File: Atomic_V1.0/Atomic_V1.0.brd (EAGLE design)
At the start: 20 x 44 mm, 17 parts

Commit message: ..
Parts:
- removed DUMMY1: (no value), Atomic_V1.0:P:EX165Y165D1651
- removed DUMMY11: (no value), Atomic_V1.0:P:EX79Y79D791
- removed DUMMY12, DUMMY13, DUMMY14, DUMMY15, DUMMY16, DUMMY17, DUMMY18, DUMMY20: (no value), Atomic_V1.0:P:RRX47Y47D331
- removed DUMMY19: (no value), Atomic_V1.0:P:SX47Y47D331
- removed DUMMY67: (no value), Atomic_V1.0:P:EX71Y71D511
- removed DUMMY68, DUMMY69: (no value), Atomic_V1.0:P:RRX71Y71D511
- removed DUMMY70: (no value), Atomic_V1.0:P:SX71Y71D511
- removed DUMMY75: (no value), Atomic_V1.0:EF154X154MID1
- removed DUMMY76: (no value), Atomic_V1.0:EF154X154MID2
- added C15: 47 nF, fliegl-wuerth:WCAP-CSGP_0402
- added C17, C19: 100 nF, fliegl-wuerth:WCAP-CSGP_0402
- added D6: 26.2V / 35pF, fliegl-wuerth:WE-TVS_SOT23-3L
- added J1: (no value), Wurth_Connectors_WR-PHD:61300411121
- added J2: (no value), Wurth_Connectors_WR-PHD:61300511121
- added R21, R22: 60.4R 1%, Resistor_smaller_fliegl:WCAP-CSRF_0402
- added U4: TLE9250VSJ, TLE9250VSJ:SOIC127P602X173-8N-V
- added X1: S4P-VH, con-JST VH:S4P-VH
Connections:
- new net +3V3: C19.1, U4.5
- new net +5V: C17.1, U4.3
- new net CAN1_RXD: U4.4
- new net CAN1_TXD: U4.1
- new net CAN_H: D6.2, R22.2, U4.7, X1.3
- new net CAN_L: D6.1, R21.1, U4.6, X1.4
- new net GND: C15.2, C17.2, C19.2, D6.3, U4.2, U4.8, X1.1
- new net N$17: C15.1, R21.2, R22.1
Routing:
- net CAN_L: track 0.00 -> 17.3 mm
- net CAN_H: track 0.00 -> 14.0 mm
- net GND: track 0.00 -> 3.31 mm, vias 0 -> 4
- net N$17: track 0.00 -> 2.54 mm
- net +5V: track 0.00 -> 2.10 mm
- net +3V3: track 0.00 -> 1.78 mm

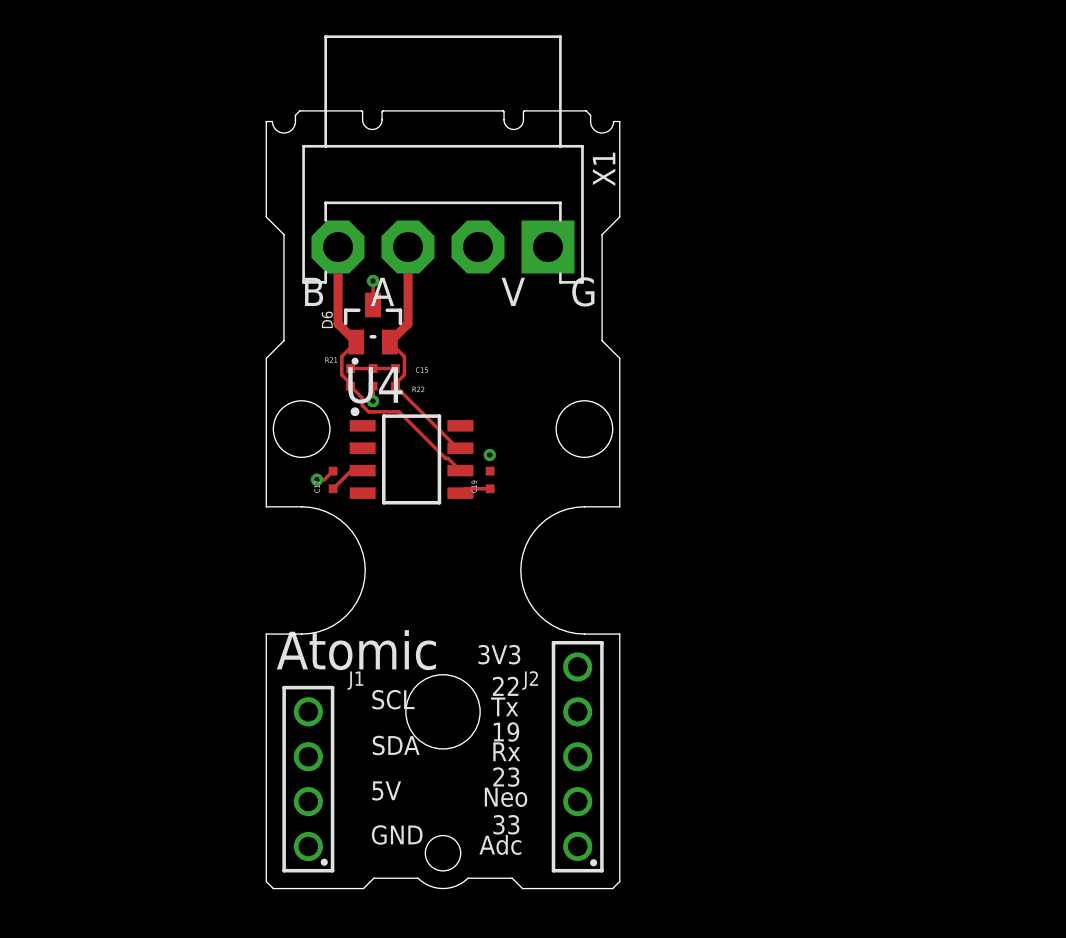
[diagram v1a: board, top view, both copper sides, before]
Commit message: 2 Airwires
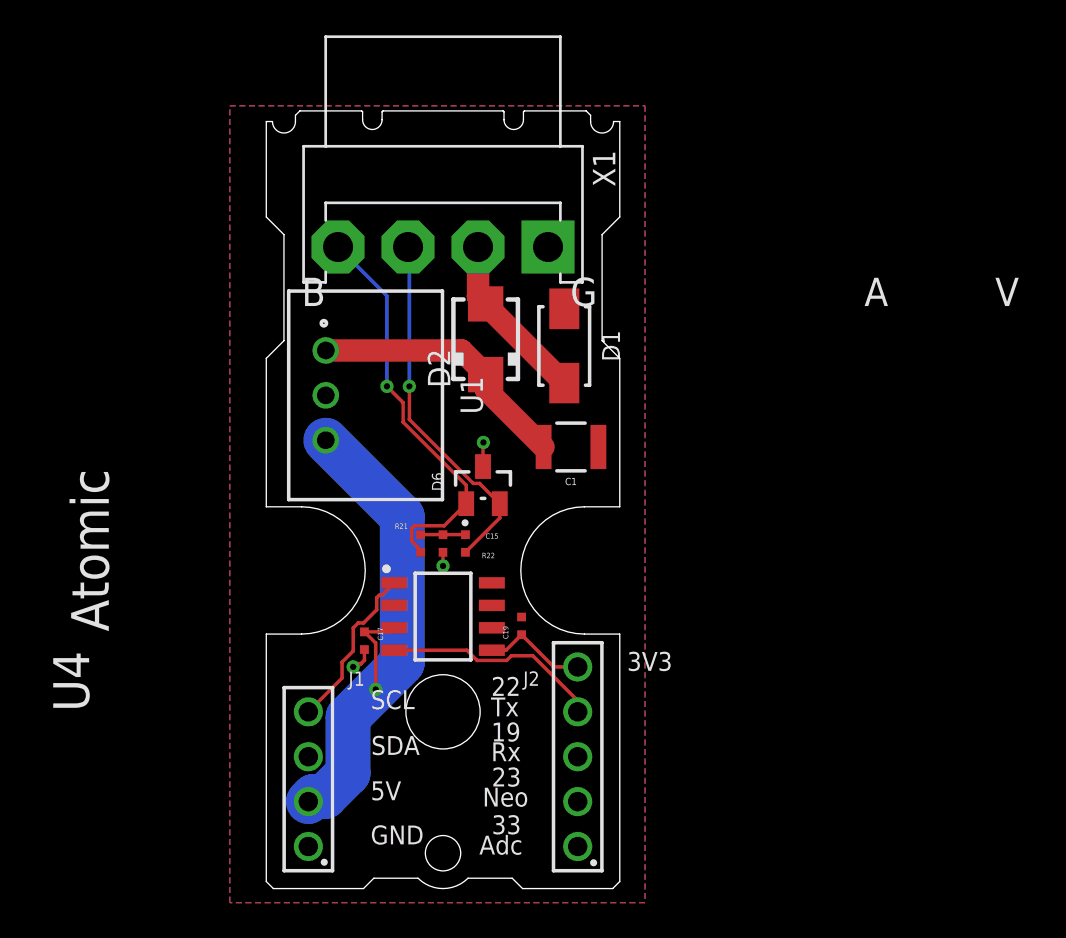
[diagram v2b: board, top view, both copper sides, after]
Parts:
- added C1: 22µF, Wurth_Capacitors_WCAP-CSGP:WCAP-CSGP_1210_H2.5
- added D1: 26V, Wurth_EMC Components_WE-TVSP:WE-TVSP_DO-214AC_BIDIRECTIONAL
- added D2: S1ML, fliegl-elektronik:SMA
- added U1: (no value), Wurth_Step Down Converter_MagI³C-FDSM:MAGI³C-FDSM_173XXXX42
- moved D6 11.1 mm to (9.88, 20.4)
- moved C15 10.2 mm to (7.62, 17.1)
- moved R21 10.2 mm to (6.35, 17.1)
- moved R22 10.2 mm to (8.89, 17.1)
- moved C17 9.27 mm to (3.17, 11.6), turned to 270 degrees
- moved U4 9.07 mm to (7.62, 13.0)
- moved C19 8.44 mm to (12.1, 12.5)
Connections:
- new net +12V: D1.2, D2.A, X1.2
- new net N$1: C1.2, D2.C, U1.1
- net +3V3: now also J2.5
- net +5V: now also J1.2, U1.3
- net CAN1_RXD: now also J2.4
- net CAN1_TXD: now also J1.4
- net GND: now also C1.1, D1.1, J1.1, U1.2
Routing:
- net +5V: track 2.10 -> 30.1 mm, vias 0 -> 1
- net N$1: track 0.00 -> 15.1 mm
- net CAN1_RXD: track 0.00 -> 12.4 mm
- net +12V: track 0.00 -> 10.3 mm
- net CAN1_TXD: track 0.00 -> 9.57 mm
- net CAN_H: track 14.0 -> 20.4 mm, vias 0 -> 1
- net CAN_L: track 17.3 -> 22.8 mm, vias 0 -> 1
- net +3V3: track 1.78 -> 5.98 mm
- net GND: track 3.31 -> 3.63 mm, vias 4 -> 3
- added copper zone on layer 1, net GND
- added copper zone on layer 16, net GND

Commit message: finish
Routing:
- net CAN_L: track 22.8 -> 30.1 mm
- net CAN_H: track 20.4 -> 24.7 mm
- net GND: track 3.63 -> 3.62 mm, vias 3 -> 42
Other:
- board text added: "G19"
- board text added: "G21"
- board text added: "G22"
- board text added: "G23"
- board text added: "G25"
- board text added: "G33"
- board text added: "H"
- board text added: "L"
- board text removed: "19"
- board text removed: "22"
- board text removed: "23"
- board text removed: "33"
- board text removed: "A"
- board text removed: "Adc"
- board text removed: "Atomic"
- board text removed: "B"
- board text removed: "Neo"
- board text removed: "Rx"
- board text removed: "SCL"
- board text removed: "SDA"
- board text removed: "Tx"

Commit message: collission avoid.
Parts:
- moved D1 13.1 mm to (1.40, 28.2), turned to 90 degrees
- moved C1 9.40 mm to (5.46, 22.5), turned to 90 degrees
- moved D6 9.09 mm to (0.85, 21.5), turned to 180 degrees
- moved U1 8.92 mm to (9.91, 25.5)
- moved D2 4.57 mm to (5.46, 28.8)
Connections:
- net CAN_H renamed CAN_P
- net CAN_L renamed CAN_N
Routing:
- net N$1: track 15.1 -> 7.76 mm
- net CAN_P: track 24.7 -> 30.5 mm
- net GND: track 3.62 -> 2.24 mm, vias 42 -> 45
- net +12V: track 10.3 -> 9.70 mm

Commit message: made PDF
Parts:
- C1: value 22µF -> 47uF
- D2: value S1ML -> SS12L R3
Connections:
- net CAN_N renamed CAN_L
- net CAN_P renamed CAN_H
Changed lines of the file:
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@@
 <attribute name="VCLAMP" value="42.1V" x="1.397" y="28.194" size="1.778" layer="27" rot="R90" display="off"/>
 </element>
-<element name="D2" library="fliegl-elektronik" package="SMA" value="S1ML" x="5.461" y="28.829" smashed="yes" rot="R90">
+<element name="D2" library="fliegl-elektronik" package="SMA" value="SS12L R3" x="5.461" y="28.829" smashed="yes" rot="R90">
 <attribute name="ARTIKEL_NR" value="505165" x="5.461" y="28.829" size="1.778" layer="27" rot="R90" display="off"/>
 <attribute name="NAME" x="3.766" y="29.242" size="0.8" layer="25" font="vector" ratio="10" rot="R180"/>
@@
 <attribute name="VALUE" x="8.326" y="27.095" size="1.27" layer="27" font="vector" ratio="10" rot="R90"/>
 </element>
-<element name="C1" library="Wurth_Capacitors_WCAP-CSGP" library_urn="urn:adsk.eagle:library:18488985" package="WCAP-CSGP_1210_H2.5" package3d_urn="urn:adsk.eagle:package:18489097/2" value="22µF" x="5.461" y="22.479" smashed="yes" rot="R90">
+<element name="C1" library="Wurth_Capacitors_WCAP-CSGP" library_urn="urn:adsk.eagle:library:18488985" package="WCAP-CSGP_1210_H2.5" package3d_urn="urn:adsk.eagle:package:18489097/2" value="47uF" x="5.461" y="22.479" smashed="yes" rot="R90">
 <attribute name="CERAMIC-TYPE" value="X5R Class II" x="5.461" y="22.479" size="1.778" layer="27" rot="R90" display="off"/>
 <attribute name="DATASHEET-URL" value="https://www.we-online.com/catalog/datasheet/885012109014.pdf" x="5.461" y="22.479" size="1.778" layer="27" rot="R90" display="off"/>
@@
 <wire x1="12.7" y1="10.795" x2="15.24" y2="8.255" width="0.2" layer="1"/>
 </signal>
-<signal name="CAN_P">
+<signal name="CAN_H">
 <contactref element="R22" pad="2"/>
 <contactref element="U4" pad="7"/>
@@
 <wire x1="9.09195" y1="18.3" x2="4.3784" y2="18.3" width="0.2" layer="1"/>
 </signal>
-<signal name="CAN_N">
+<signal name="CAN_L">
 <contactref element="R21" pad="1"/>
 <contactref element="U4" pad="6"/>

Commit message: done Linear Regulator Version.
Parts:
- removed D2: SS12L R3, fliegl-elektronik:SMA
- removed U1: (no value), Wurth_Step Down Converter_MagI³C-FDSM:MAGI³C-FDSM_173XXXX42
- added C2: 100 nF, fliegl-wuerth:WCAP-CSGP_0402
- added C3: 22 µF, Wurth_Capacitors_WCAP-CSGP:WCAP-CSGP_0805_H1.25_R
- added G1: TLE4270-2D-INF-PG-TO252-5-11_L_1, INF-PG-TO252-5-11L:INF-PG-TO252-5-11_L_1PRIMARY
- moved D1 5.59 mm to (6.58, 30.3), turned to 0 degrees
- moved C1 4.57 mm to (7.11, 26.7), turned to 0 degrees
- moved D6 2.80 mm to (3.56, 22.2), turned to 90 degrees
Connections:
- net +12V: now also C1.2, G1.1; no longer D2.A
- net +5V: now also C3.2, G1.5; no longer U1.3
- net GND: now also C2.2, C3.1, G1.3; no longer U1.2
- net N$1: now also C2.1, G1.4; no longer C1.2, D2.C, U1.1
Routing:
- net GND: track 2.24 -> 12.2 mm, vias 45 -> 97
- net +5V: track 30.2 -> 37.0 mm, vias 1 -> 4
- net +12V: track 9.70 -> 13.8 mm
- net CAN_L: track 30.6 -> 33.7 mm
- net N$1: track 7.76 -> 5.92 mm
- net CAN_H: track 30.5 -> 29.4 mm
